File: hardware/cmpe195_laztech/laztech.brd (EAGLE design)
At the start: 100 x 80 mm, 6 parts

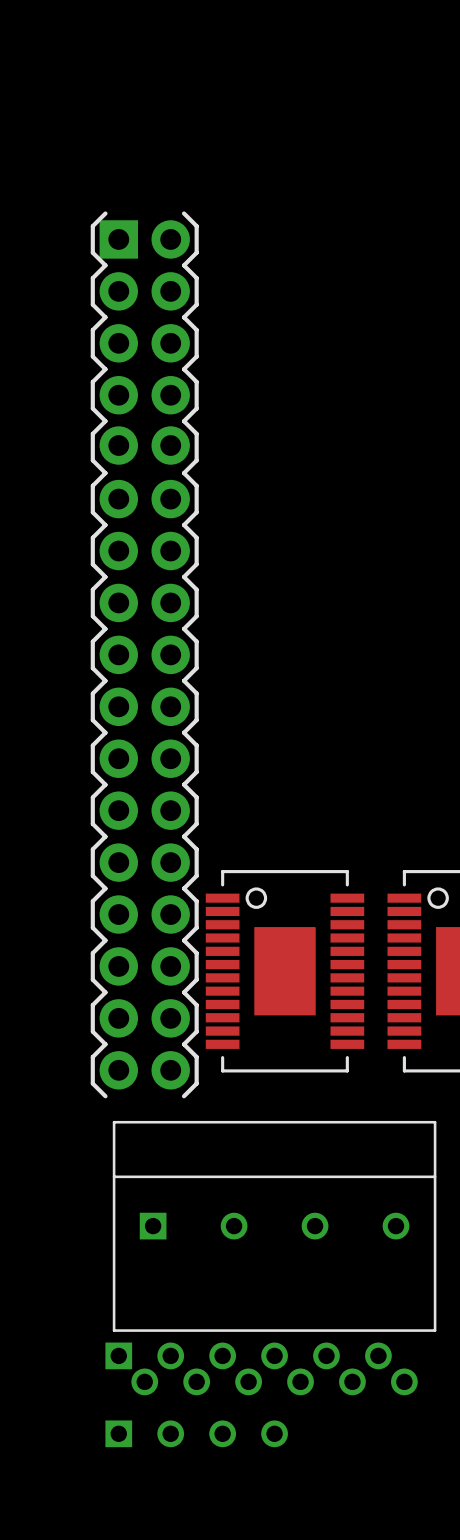
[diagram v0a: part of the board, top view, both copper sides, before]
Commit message: Added initial direct connections with no passives.
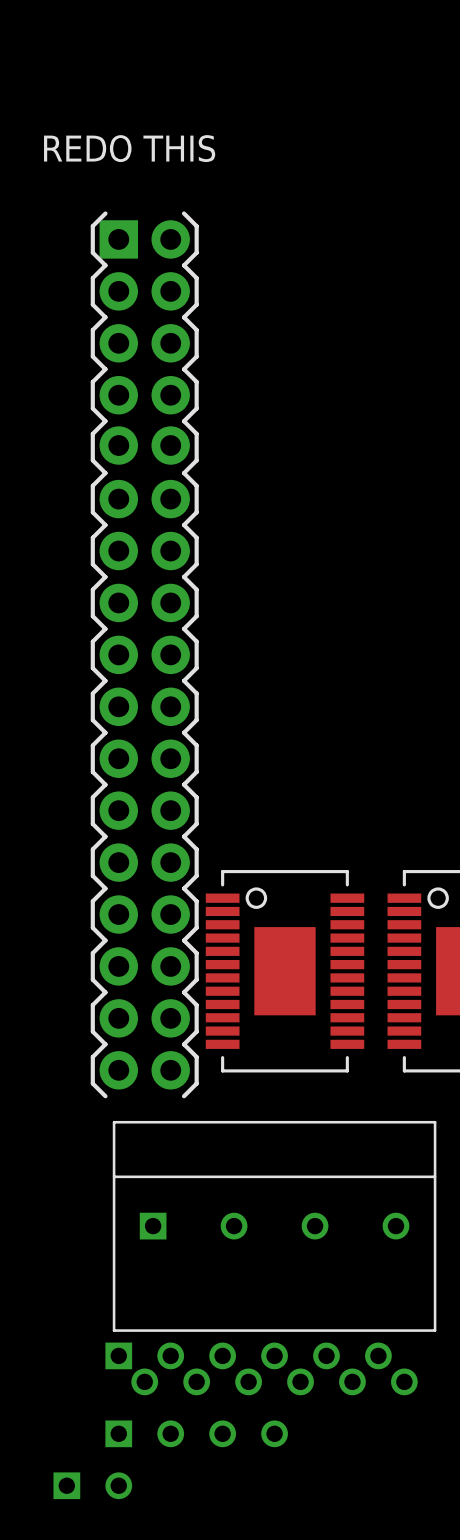
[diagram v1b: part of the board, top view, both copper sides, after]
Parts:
- added U$7: SJSUONEVIN, laztech_parts:M1X2
- U$1, U$2: device laztech_parts:TSSOP-24P -> laztech_parts:ETSSOP-24
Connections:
- new net +3V3: U$3.34
- new net +5V: U$1.10, U$2.10, U$4.2, U$5.10, U$7.1
- new net GND: U$1.13, U$1.24, U$1.25, U$2.13, U$2.24, U$2.25, U$3.17, U$3.33, U$4.3, U$5.7, U$7.2
- new net N$20: U$2.23, U$3.13
- new net N$21: U$2.7, U$3.12
- new net N$22: U$2.9, U$3.14
- new net N$23: U$1.7, U$3.9
- new net N$24: U$1.23, U$3.10
- new net N$25: U$1.9, U$3.11
- net N$1: now also U$5.1; no longer U$5.P$1
- net N$10: now also U$5.9; no longer U$5.P$9
- net N$11: now also U$5.8; no longer U$5.P$8
- net N$2: now also U$5.2; no longer U$5.P$2
- net N$3: now also U$5.3; no longer U$5.P$3
- net N$4: now also U$5.4; no longer U$5.P$4
- net N$5: now also U$6.1; no longer U$6.P$1
- net N$6: now also U$6.2; no longer U$6.P$2
- net N$7: now also U$6.3; no longer U$6.P$3
- net N$8: now also U$6.4; no longer U$6.P$4
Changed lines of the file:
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@@
 </autorouter>
 <elements>
-<element name="U$1" library="laztech_parts" package="TSSOP-24P" value="A4985SLPTR-T" x="-7.62" y="-43.18"/>
-<element name="U$2" library="laztech_parts" package="TSSOP-24P" value="A4985SLPTR-T" x="-16.51" y="-43.18"/>
+<element name="U$1" library="laztech_parts" package="ETSSOP-24" value="A4985SLPTR-T" x="-7.62" y="-43.18"/>
+<element name="U$2" library="laztech_parts" package="ETSSOP-24" value="A4985SLPTR-T" x="-16.51" y="-43.18"/>
 <element name="U$3" library="laztech_parts" package="SJSUONEX" value="SJSUONE" x="-21.59" y="-44.45"/>
 <element name="U$4" library="laztech_parts" package="KK396-4" value="K40KK" x="-13.97" y="-52.07"/>
 <element name="U$5" library="laztech_parts" package="FFC-12" value="K40FFC" x="-21.59" y="-58.42"/>
 <element name="U$6" library="laztech_parts" package="JST-4" value="K40JST" x="-21.59" y="-62.23"/>
+<element name="U$7" library="laztech_parts" package="M1X2" value="SJSUONEVIN" x="-24.13" y="-64.77"/>
 </elements>
 <signals>
 <signal name="N$1">
 <contactref element="U$1" pad="18"/>
-<contactref element="U$5" pad="P$1"/>
+<contactref element="U$5" pad="1"/>
 <wire x1="-1.52" y1="-39.93" x2="-21.59" y2="-58.42" width="0" layer="19" extent="1-1"/>
 </signal>
 <signal name="N$2">
 <contactref element="U$1" pad="15"/>
-<contactref element="U$5" pad="P$2"/>
+<contactref element="U$5" pad="2"/>
 <wire x1="-1.52" y1="-41.88" x2="-20.32" y2="-59.69" width="0" layer="19" extent="1-1"/>
 </signal>
 <signal name="N$3">
 <contactref element="U$1" pad="19"/>
-<contactref element="U$5" pad="P$3"/>
+<contactref element="U$5" pad="3"/>
 <wire x1="-1.52" y1="-39.28" x2="-19.05" y2="-58.42" width="0" layer="19" extent="1-1"/>
 </signal>
 <signal name="N$4">
 <contactref element="U$1" pad="22"/>
-<contactref element="U$5" pad="P$4"/>
+<contactref element="U$5" pad="4"/>
 <wire x1="-1.52" y1="-37.33" x2="-17.78" y2="-59.69" width="0" layer="19" extent="1-1"/>
 </signal>
 <signal name="N$5">
 <contactref element="U$2" pad="18"/>
-<contactref element="U$6" pad="P$1"/>
+<contactref element="U$6" pad="1"/>
 <wire x1="-10.41" y1="-39.93" x2="-21.59" y2="-62.23" width="0" layer="19" extent="1-1"/>
 </signal>
 <signal name="N$6">
 <contactref element="U$2" pad="15"/>
-<contactref element="U$6" pad="P$2"/>
+<contactref element="U$6" pad="2"/>
 <wire x1="-10.41" y1="-41.88" x2="-19.05" y2="-62.23" width="0" layer="19" extent="1-1"/>
 </signal>
 <signal name="N$7">
 <contactref element="U$2" pad="19"/>
-<contactref element="U$6" pad="P$3"/>
+<contactref element="U$6" pad="3"/>
 <wire x1="-10.41" y1="-39.28" x2="-16.51" y2="-62.23" width="0" layer="19" extent="1-1"/>
 </signal>
 <signal name="N$8">
 <contactref element="U$2" pad="22"/>
-<contactref element="U$6" pad="P$4"/>
+<contactref element="U$6" pad="4"/>
 <wire x1="-10.41" y1="-37.33" x2="-13.97" y2="-62.23" width="0" layer="19" extent="1-1"/>
 </signal>
@@
 </signal>
 <signal name="N$10">
-<contactref element="U$5" pad="P$9"/>
+<contactref element="U$5" pad="9"/>
 <contactref element="U$3" pad="7"/>
 <wire x1="-21.59" y1="-19.05" x2="-11.43" y2="-58.42" width="0" layer="19" extent="1-1"/>
 </signal>
 <signal name="N$11">
-<contactref element="U$5" pad="P$8"/>
+<contactref element="U$5" pad="8"/>
 <contactref element="U$3" pad="8"/>
 <wire x1="-21.59" y1="-21.59" x2="-12.7" y2="-59.69" width="0" layer="19" extent="1-1"/>
@@
 <wire x1="-19.05" y1="-16.51" x2="-1.52" y2="-42.53" width="0" layer="19" extent="1-1"/>
 </signal>
+<signal name="N$20">
+<contactref element="U$2" pad="23"/>
+<contactref element="U$3" pad="13"/>
+<wire x1="-10.41" y1="-36.68" x2="-21.59" y2="-34.29" width="0" layer="19" extent="1-1"/>
+</signal>
+<signal name="N$21">
+<contactref element="U$2" pad="7"/>
+<contactref element="U$3" pad="12"/>
+<wire x1="-21.59" y1="-31.75" x2="-16.51" y2="-39.93" width="0" layer="19" extent="1-1"/>
+</signal>
+<signal name="N$22">
+<contactref element="U$2" pad="9"/>
+<contactref element="U$3" pad="14"/>
+<wire x1="-21.59" y1="-36.83" x2="-16.51" y2="-41.23" width="0" layer="19" extent="1-1"/>
+</signal>
+<signal name="N$23">
+<contactref element="U$3" pad="9"/>
+<contactref element="U$1" pad="7"/>
+<wire x1="-21.59" y1="-24.13" x2="-7.62" y2="-39.93" width="0" layer="19" extent="1-1"/>
+</signal>
+<signal name="N$24">
+<contactref element="U$3" pad="10"/>
+<contactref element="U$1" pad="23"/>
+<wire x1="-1.52" y1="-36.68" x2="-21.59" y2="-26.67" width="0" layer="19" extent="1-1"/>
+</signal>
+<signal name="N$25">
+<contactref element="U$3" pad="11"/>
+<contactref element="U$1" pad="9"/>
+<wire x1="-7.62" y1="-41.23" x2="-21.59" y2="-29.21" width="0" layer="19" extent="1-1"/>
+</signal>
+<signal name="GND">
+<contactref element="U$3" pad="33"/>
+<contactref element="U$3" pad="17"/>
+<contactref element="U$5" pad="7"/>
+<contactref element="U$4" pad="3"/>
+<contactref element="U$2" pad="13"/>
+<contactref element="U$2" pad="24"/>
+<contactref element="U$2" pad="25"/>
+<contactref element="U$1" pad="13"/>
+<contactref element="U$1" pad="24"/>
+<contactref element="U$1" pad="25"/>
+<contactref element="U$7" pad="2"/>
+<wire x1="-13.97" y1="-58.42" x2="-21.59" y2="-64.77" width="0" layer="19" extent="1-1"/>
+<wire x1="-11.99" y1="-52.07" x2="-13.97" y2="-58.42" width="0" layer="19" extent="1-1"/>
+<wire x1="-10.41" y1="-43.18" x2="-11.99" y2="-52.07" width="0" layer="19" extent="1-1"/>
+<wire x1="-13.46" y1="-39.605" x2="-10.41" y2="-43.18" width="0" layer="19" extent="1-1"/>
+<wire x1="-10.41" y1="-36.03" x2="-13.46" y2="-39.605" width="0" layer="19" extent="1-1"/>
+<wire x1="-4.57" y1="-39.605" x2="-10.41" y2="-43.18" width="0" layer="19" extent="1-1"/>
+<wire x1="-1.52" y1="-43.18" x2="-4.57" y2="-39.605" width="0" layer="19" extent="1-1"/>
+<wire x1="-1.52" y1="-36.03" x2="-4.57" y2="-39.605" width="0" layer="19" extent="1-1"/>
+<wire x1="-21.59" y1="-44.45" x2="-13.46" y2="-39.605" width="0" layer="19" extent="1-1"/>
+<wire x1="-19.05" y1="-6.35" x2="-10.41" y2="-36.03" width="0" layer="19" extent="1-1"/>
+</signal>
+<signal name="+3V3">
+<contactref element="U$3" pad="34"/>
+</signal>
+<signal name="+5V">
+<contactref element="U$2" pad="10"/>
+<contactref element="U$1" pad="10"/>
+<contactref element="U$4" pad="2"/>
+<contactref element="U$5" pad="10"/>
+<contactref element="U$7" pad="1"/>
+<wire x1="-10.16" y1="-59.69" x2="-24.13" y2="-64.77" width="0" layer="19" extent="1-1"/>
+<wire x1="-15.95" y1="-52.07" x2="-10.16" y2="-59.69" width="0" layer="19" extent="1-1"/>
+<wire x1="-16.51" y1="-41.88" x2="-15.95" y2="-52.07" width="0" layer="19" extent="1-1"/>
+<wire x1="-7.62" y1="-41.88" x2="-16.51" y2="-41.88" width="0" layer="19" extent="1-1"/>
+</signal>
 </signals>

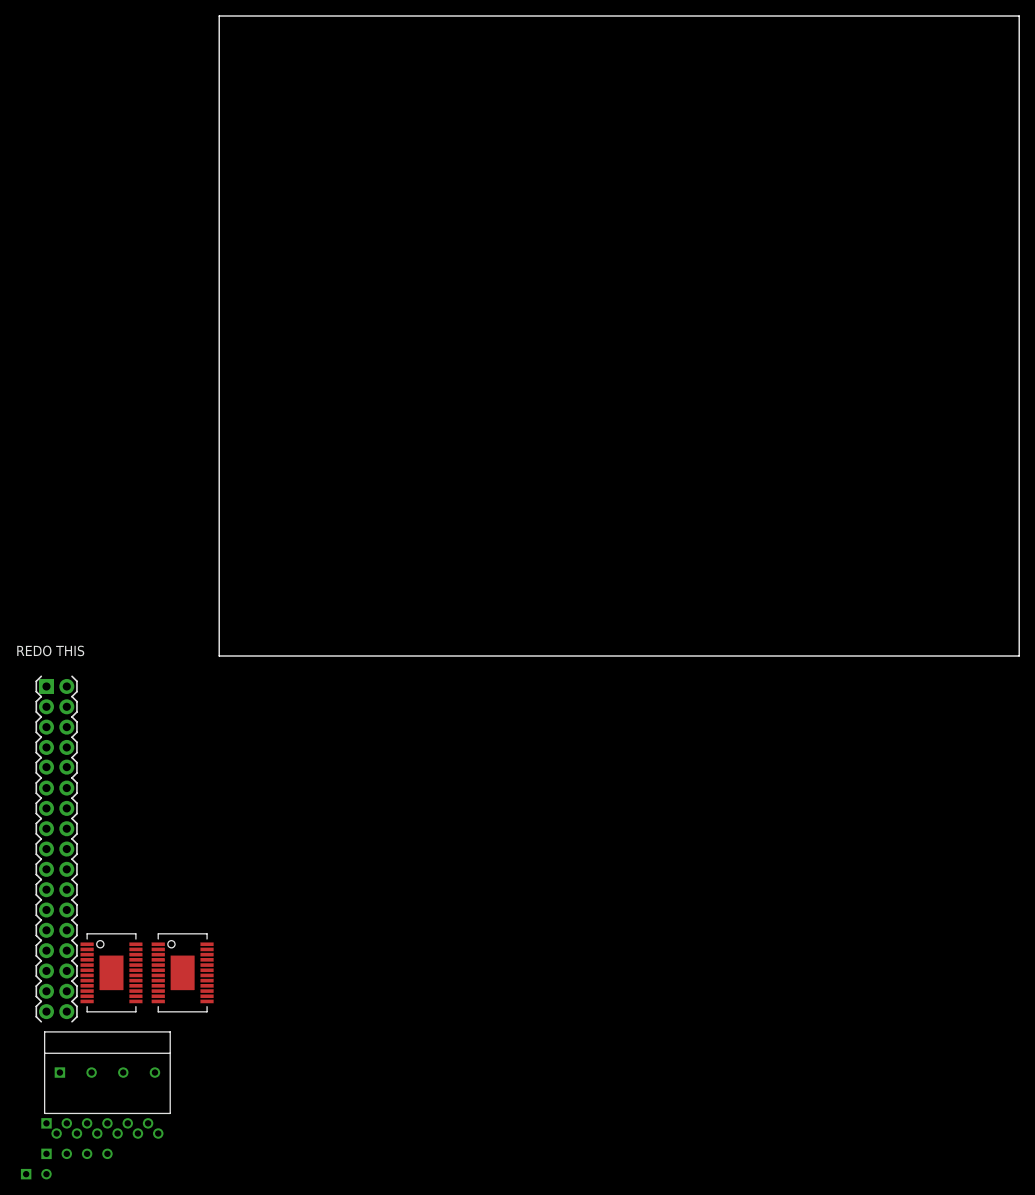
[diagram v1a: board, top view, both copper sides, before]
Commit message: Started board layout and added Rosc to ground.
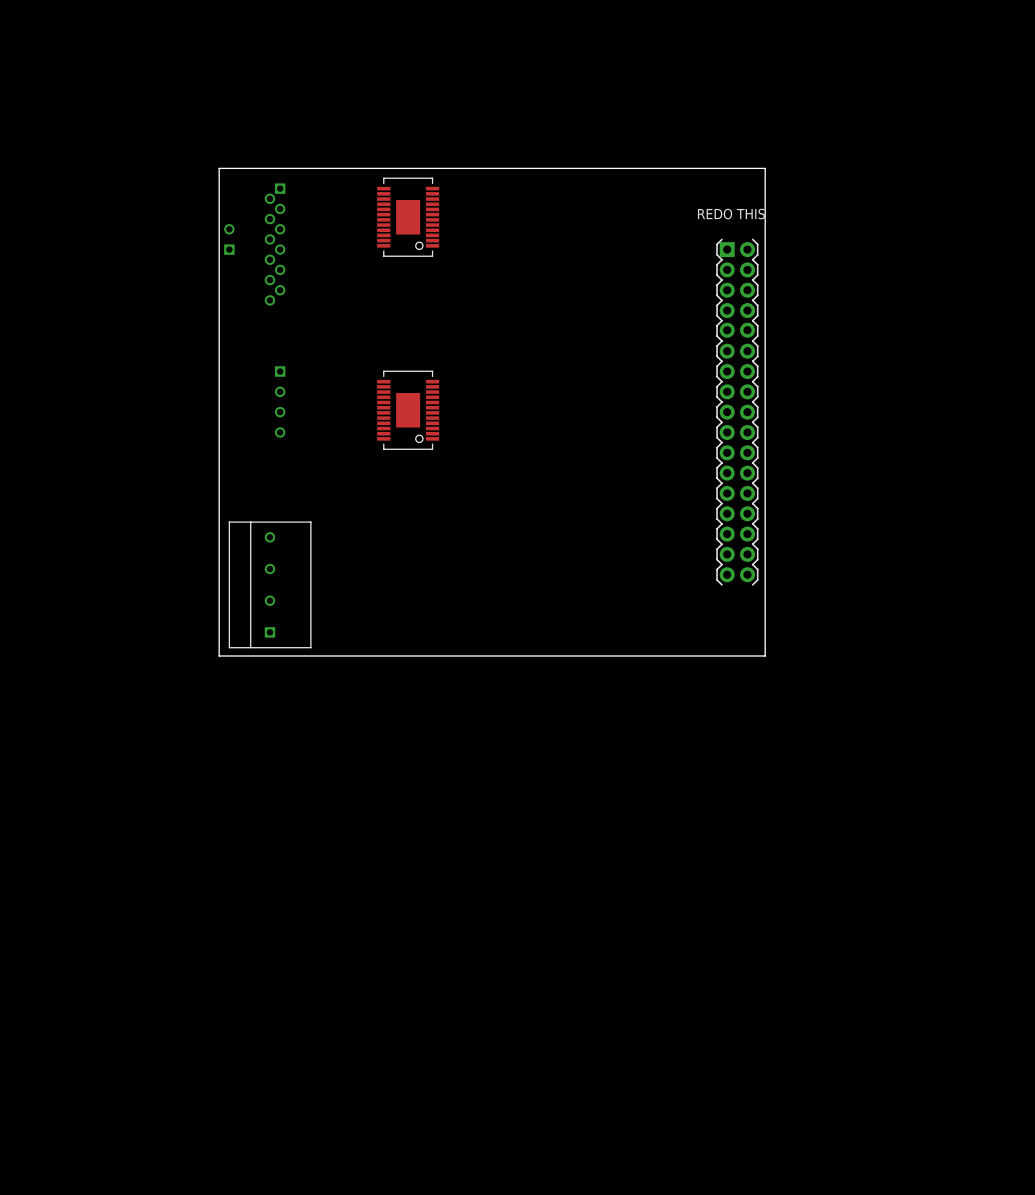
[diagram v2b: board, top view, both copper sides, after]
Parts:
- moved U$5 120.4 mm to (7.62, 58.4), turned to 270 degrees
- moved U$7 118.3 mm to (1.27, 50.8), turned to 90 degrees
- moved U$1 107.2 mm to (26.7, 58.4), turned to 180 degrees
- moved U$6 102.1 mm to (7.62, 35.6), turned to 270 degrees
- moved U$3 101.1 mm to (63.5, 10.2)
- moved U$2 88.7 mm to (26.7, 34.3), turned to 180 degrees
- moved U$4 64.3 mm to (6.35, 8.89), turned to 90 degrees
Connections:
- net +3V3: now also U$1.10, U$2.10
- net +5V: no longer U$1.10, U$2.10
- net GND: now also U$1.8, U$2.8
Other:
- board size 100 x 80 mm -> 68.2 x 61 mm

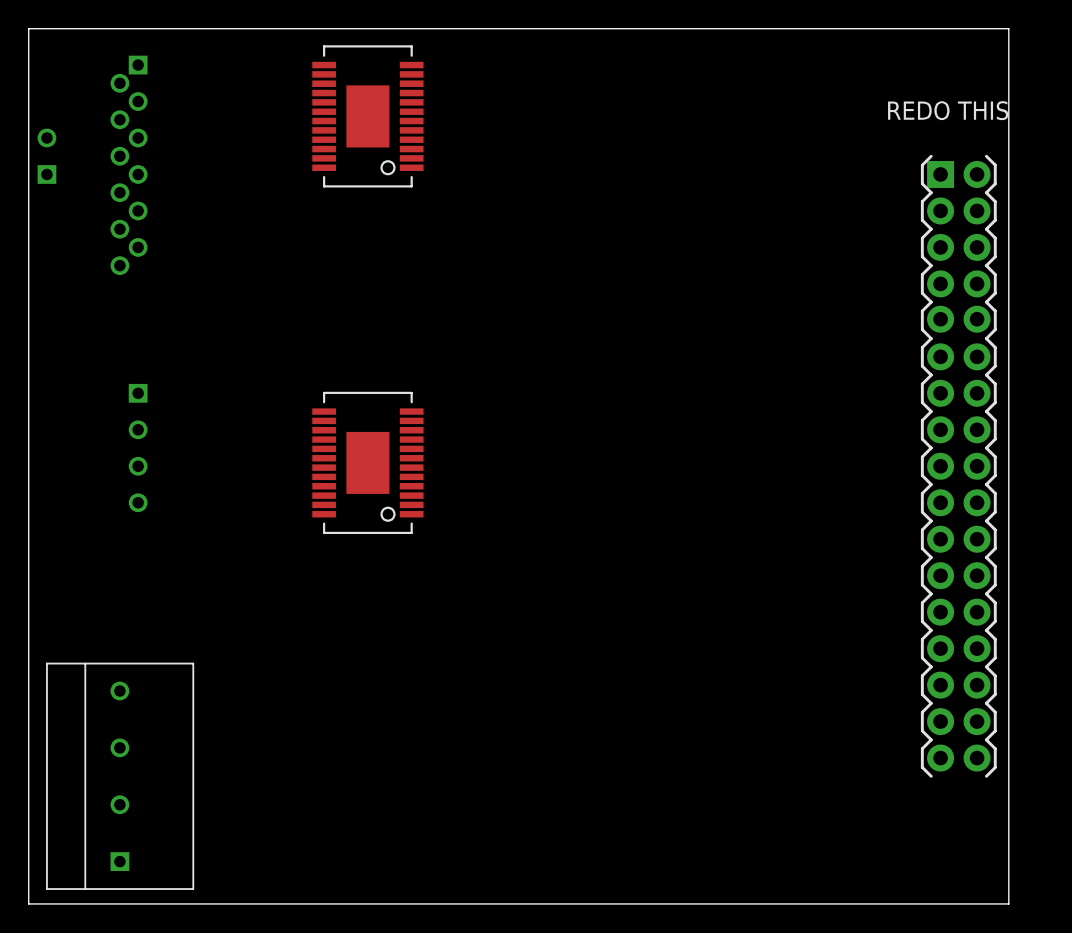
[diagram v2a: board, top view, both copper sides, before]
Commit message: Replaced some connectors with SFE connecters.
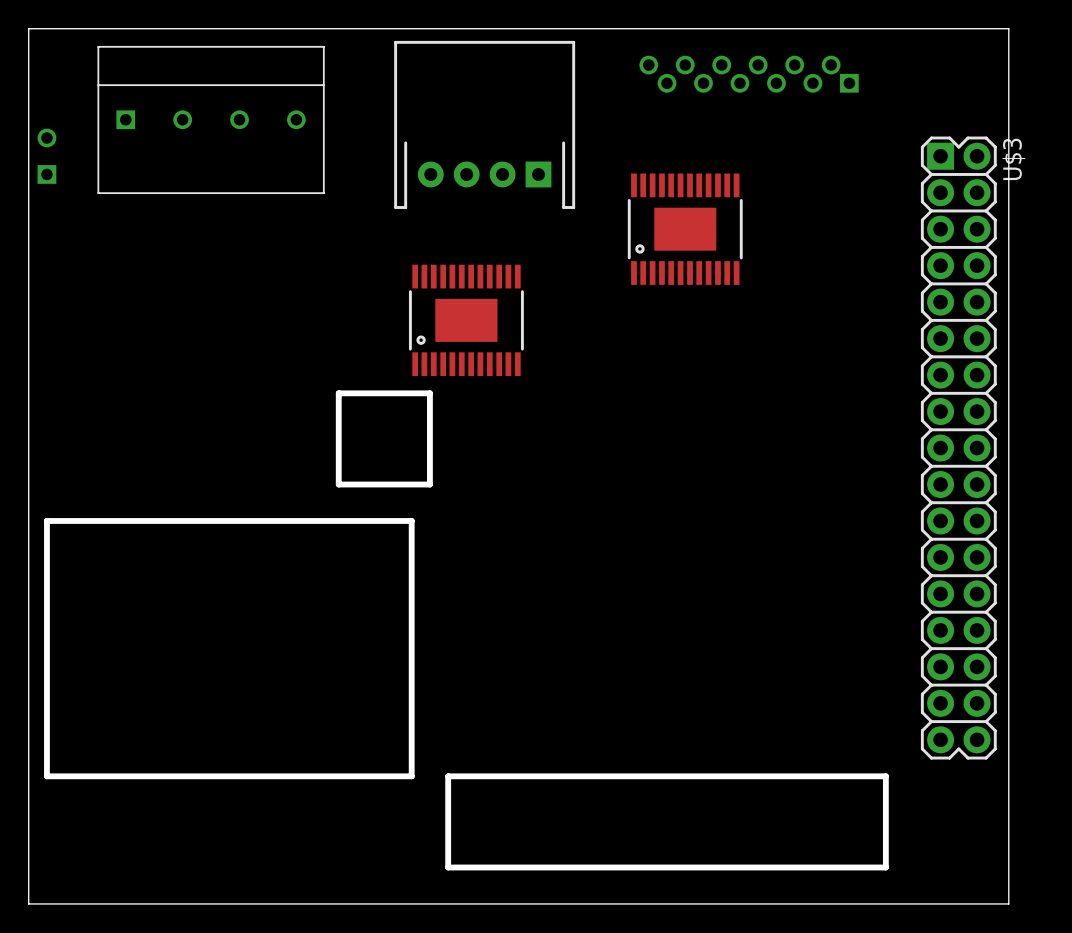
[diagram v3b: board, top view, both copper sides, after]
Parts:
- U$1, U$2: device laztech_parts:ETSSOP-24 -> laztech_parts:TSSOP-24
- U$3: value SJSUONE -> SJSUONEX; device laztech_parts:SJSUONEX -> laztech_parts:2X17
- U$6: device laztech_parts:JST-4 -> laztech_parts:JST-XH-4-RA
- moved U$5 49.5 mm to (57.1, 57.1), turned to 180 degrees
- moved U$4 46.2 mm to (12.7, 54.6), turned to 0 degrees
- moved U$6 28.5 mm to (31.8, 50.8), turned to 0 degrees
- moved U$1 22.2 mm to (45.7, 47.0), turned to 0 degrees
- moved U$3 21.6 mm to (64.8, 31.8), turned to 270 degrees
- moved U$2 7.41 mm to (30.5, 40.6), turned to 0 degrees
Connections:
- net +5V: now also U$5.3; no longer U$5.10
- net GND: now also U$1.EP, U$2.EP, U$5.6; no longer U$1.25, U$2.25, U$5.7
- net N$1: now also U$5.9; no longer U$5.1
- net N$10: now also U$5.5; no longer U$5.9
- net N$11: now also U$5.4; no longer U$5.8
- net N$2: now also U$5.10; no longer U$5.2
- net N$3: now also U$5.11; no longer U$5.3
- net N$4: now also U$5.12; no longer U$5.4
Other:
- outline, holes or cut-outs redrawn
